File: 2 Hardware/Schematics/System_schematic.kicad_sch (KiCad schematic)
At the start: 9 parts, among them M1 Motor_Servo 180, M2 Motor_Servo 360, U1 TSDP341xx (Infrared Data Rece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

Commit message: Lots of CAD - completed the Gun model (Asthetics left only). Hardware:added a page to main schematic to show number of wires needed for rotating plate. Software : re-create software project
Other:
- added sheet PositionOfComponents (PositionOfComponents.kicad_sch)

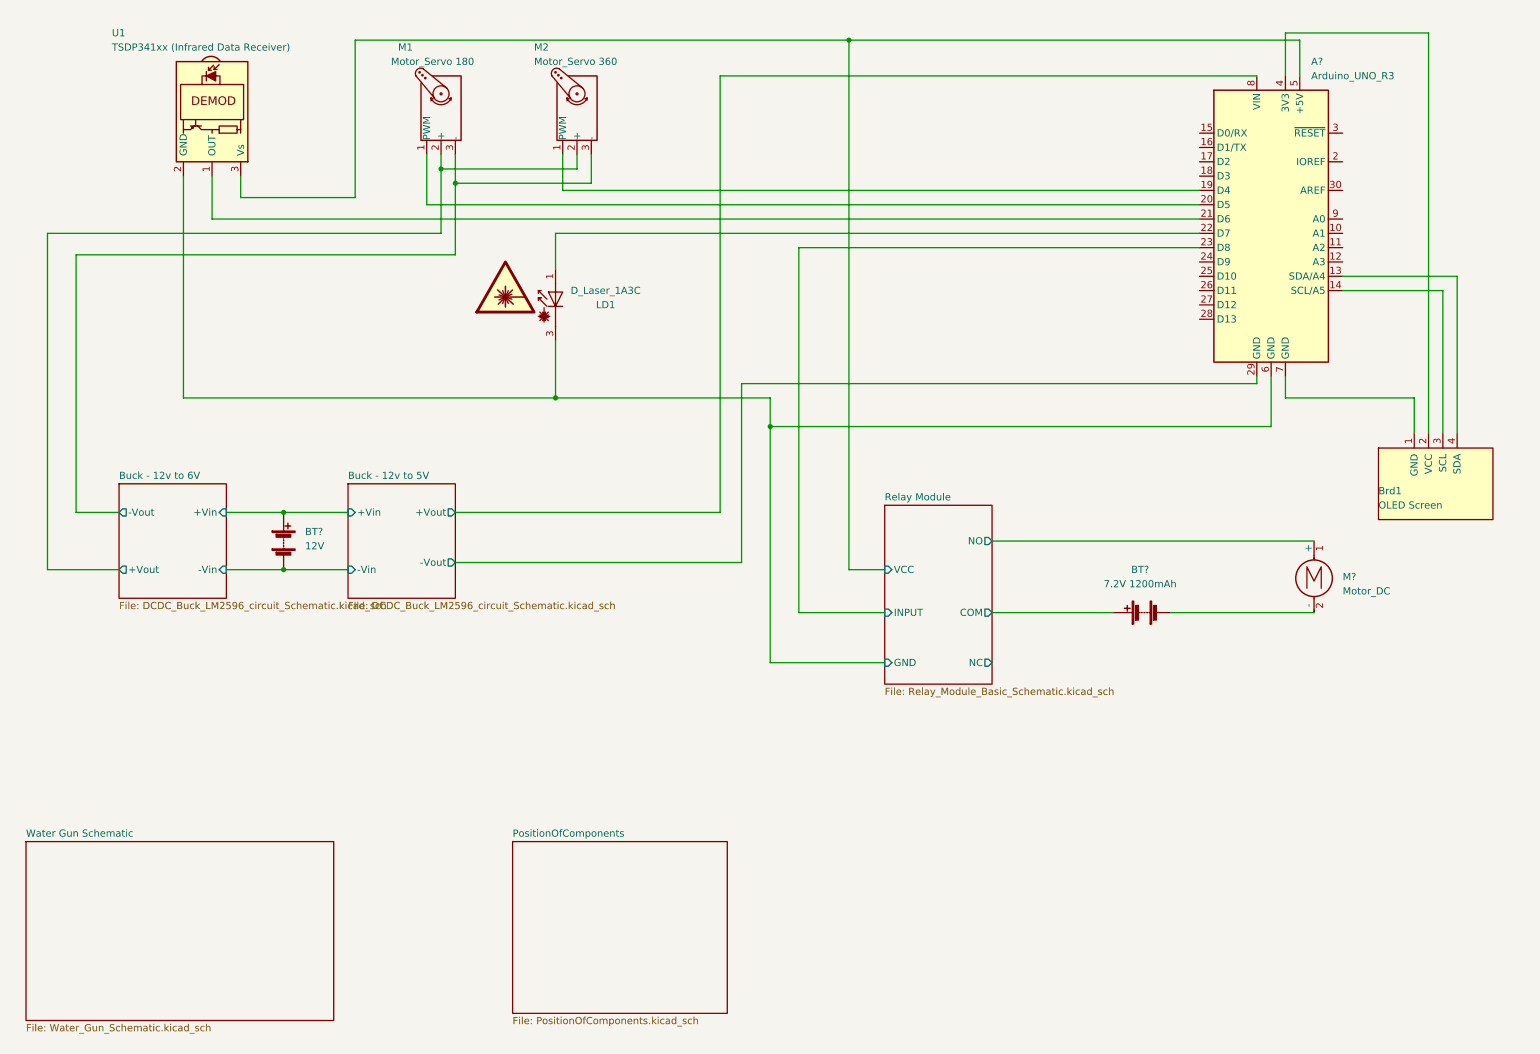
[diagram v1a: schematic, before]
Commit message: HW:Schematic changes(ESP-32), CAD:Fixes to tower + cleanup, SW: Initial State machine diagram made. Added drawing notes of mechanics calculations
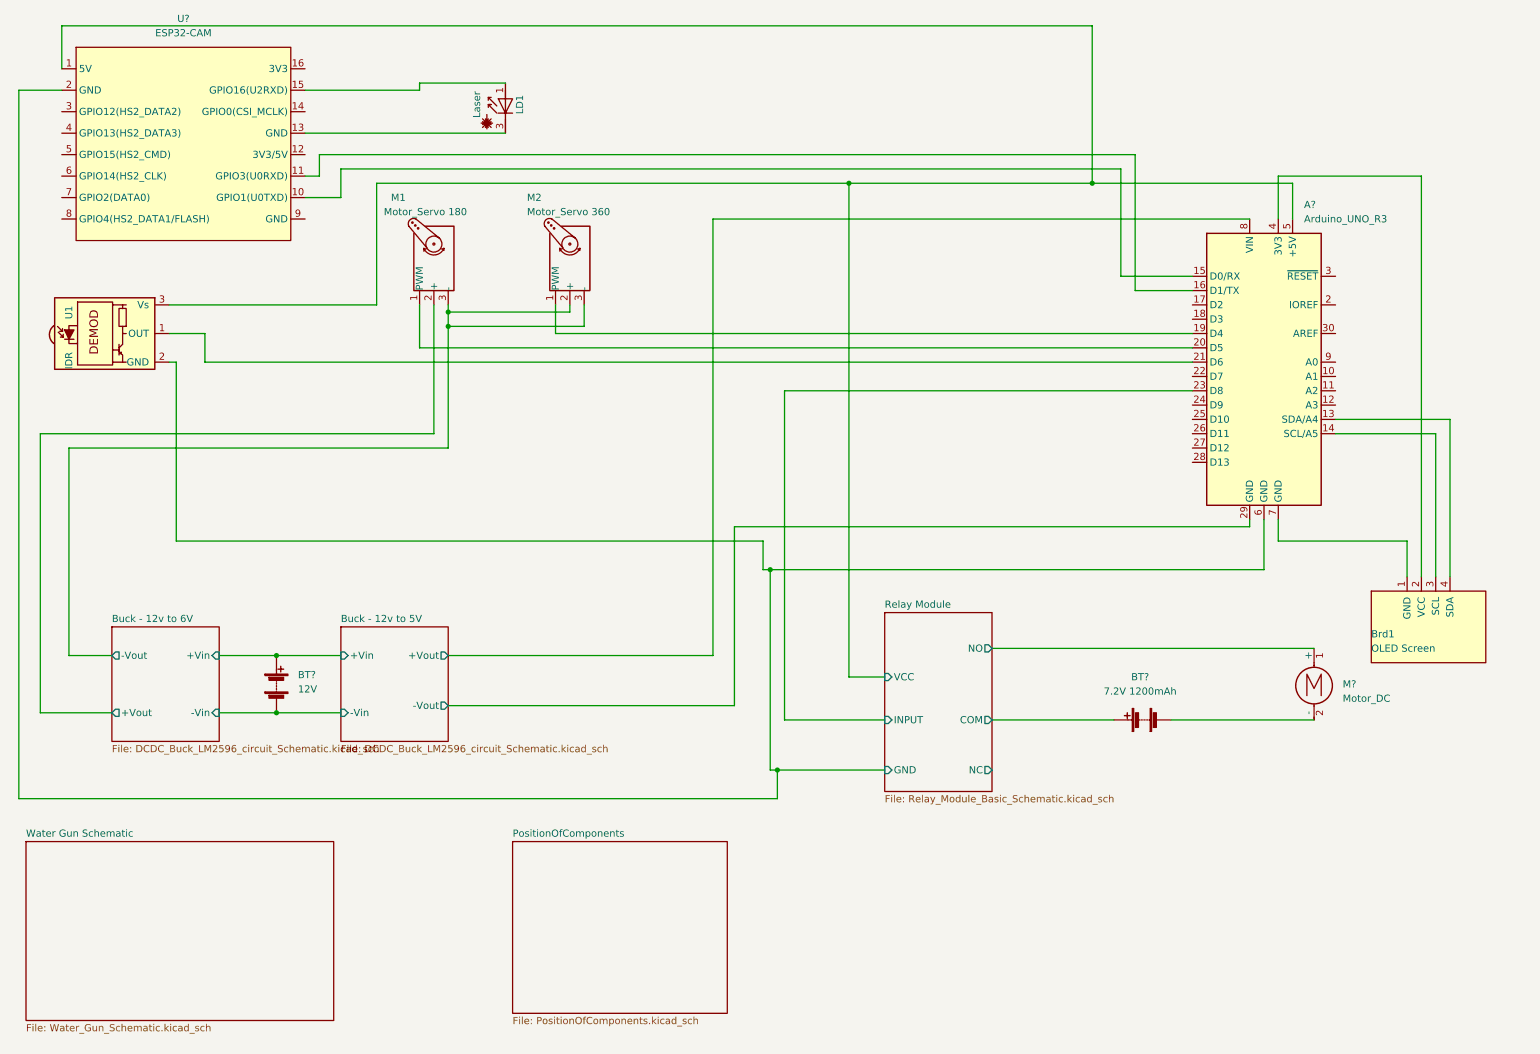
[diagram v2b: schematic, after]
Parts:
- added U?: ESP32-CAM, symbol Custom_Lib:ESP32-CAM
- LD1: value D_Laser_1A3C -> Laser
- U1: value TSDP341xx (Infrared Data Receiver) -> IDR
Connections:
- net Buck - 12v to 6V/+Vout: no longer M2.2 (+)
- net Buck - 12v to 6V/-Vout: now also M2.2 (+)
- net Relay Module/GND: now also U?.2 (GND); no longer LD1.3 (K)
- net Relay Module/VCC: now also U?.1 (5V)
- net at LD1.1 (A): now also U?.15 (GPIO16(U2RXD)); no longer A?.22 (D7)
- net at A?.15 (D0/RX): now also U?.10 (GPIO1(U0TXD))
- net at A?.16 (D1/TX): now also U?.11 (GPIO3(U0RXD))
- new net: LD1.3 (K), U?.13 (GND)
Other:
- moved on the sheet: A?, BT?, Brd1, LD1, M1, M2, M?, U1

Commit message: Have added the ESP-32 and reorginised the schematic
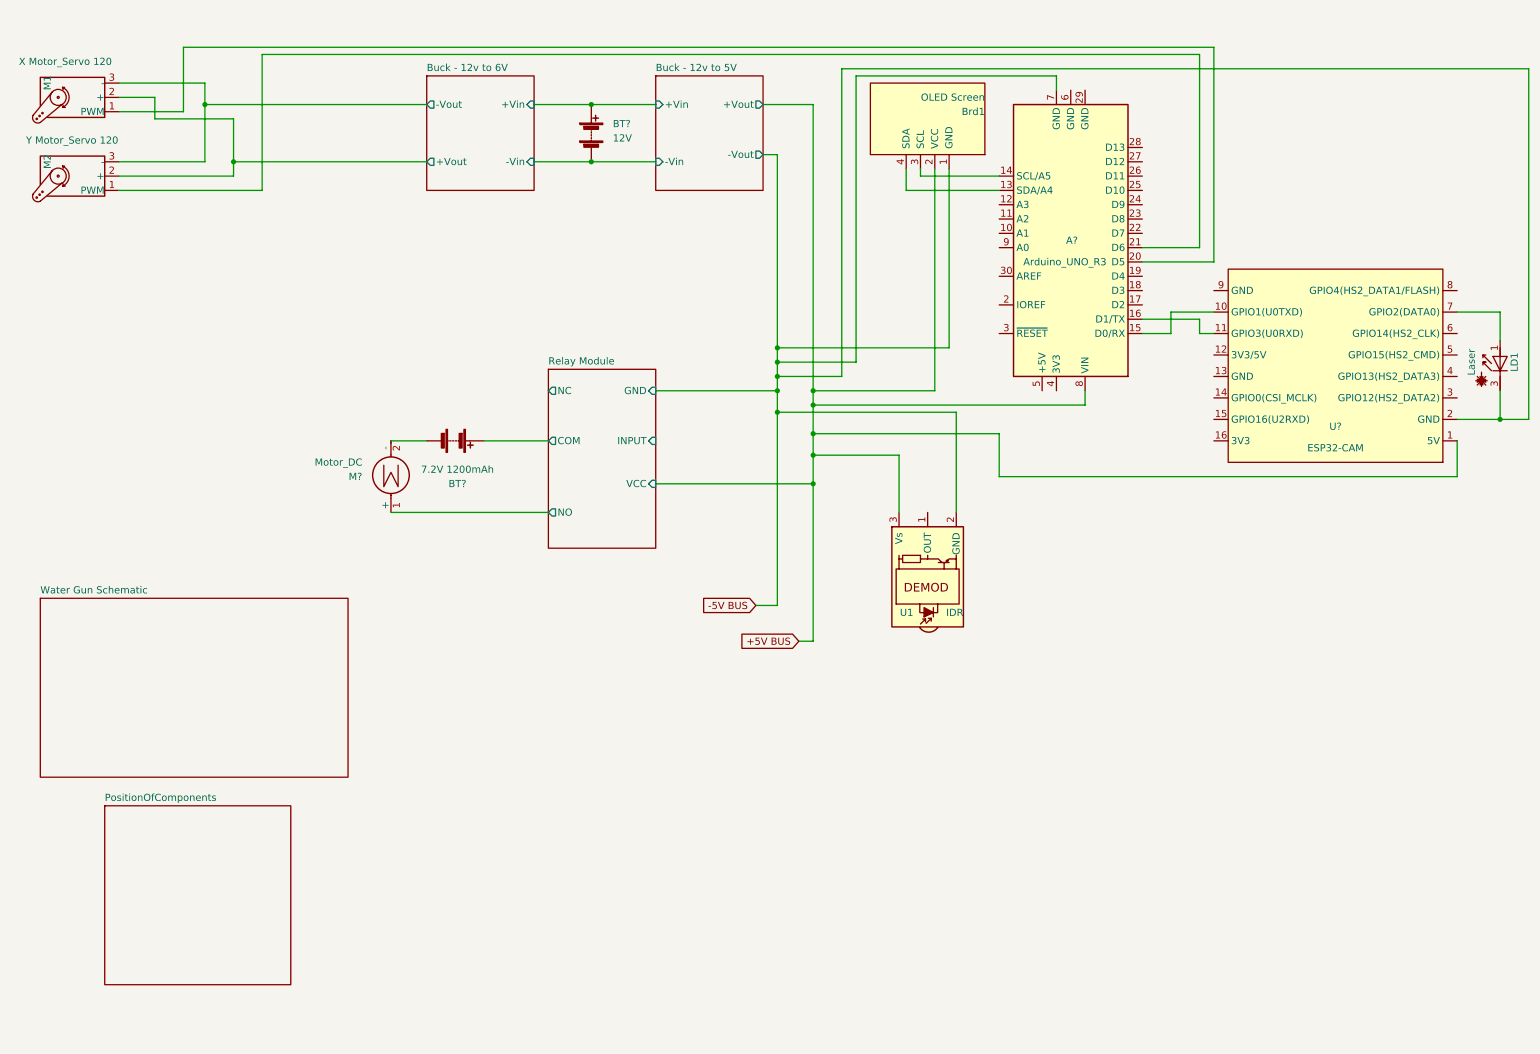
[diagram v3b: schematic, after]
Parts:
- M1: value Motor_Servo 180 -> X Motor_Servo 120
- M2: value Motor_Servo 360 -> Y Motor_Servo 120
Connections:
- net Buck - 12v to 6V/+Vout: now also M2.2 (+)
- net Buck - 12v to 6V/-Vout: no longer M2.2 (+)
- net Relay Module/INPUT: no longer A?.23 (D8)
- net -5V BUS: now reaches A?.7 (GND), Brd1.1 (GND)
- net -5V BUS: now also LD1.3 (K), U1.2 (GND), U?.2 (GND)
- net at A?.4 (3V3): no longer Brd1.2 (VCC)
- net at LD1.1 (A): now also U?.7 (GPIO2(DATA0)); no longer U?.15 (GPIO16(U2RXD))
- net at U?.13 (GND): no longer LD1.3 (K)
- net at A?.19 (D4): no longer M2.1 (PWM)
- net at A?.21 (D6): now also M2.1 (PWM); no longer U1.1 (OUT)
- net Buck - 12v to 5V/+Vout renamed +5V BUS
- net +5V BUS: now also Brd1.2 (VCC), U1.3 (Vs), U?.1 (5V)
- net Buck - 12v to 5V/-Vout: no longer names the net of A?.29 (GND)
- removed net Relay Module/GND: A?.6 (GND), U1.2 (GND), U?.2 (GND)
- removed net Relay Module/VCC: A?.5 (+5V), U1.3 (Vs), U?.1 (5V)
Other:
- moved on the sheet: A?, BT?, Brd1, LD1, M1, M2, M?, U1, U?

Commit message: Added gitignre, changes (minor) to schematic, changes to horizontal model (WithWheels) and general repo cleanup
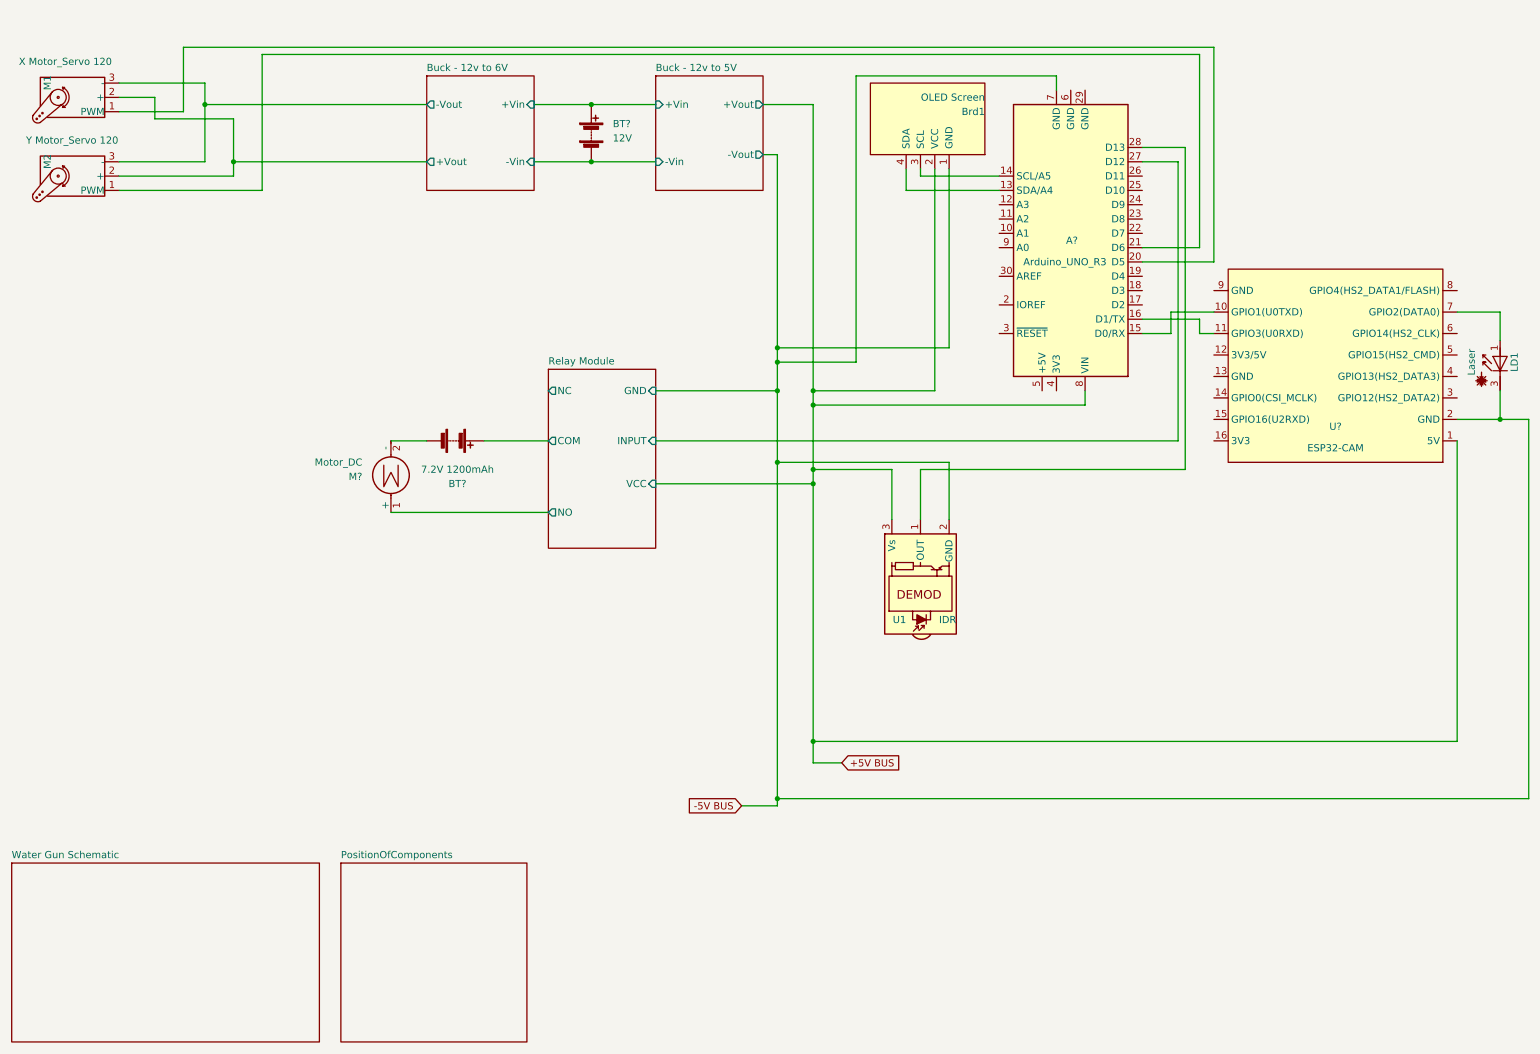
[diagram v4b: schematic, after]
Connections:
- net Relay Module/INPUT: now also A?.27 (D12)
- net at A?.28 (D13): now also U1.1 (OUT)
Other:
- moved on the sheet: U1
